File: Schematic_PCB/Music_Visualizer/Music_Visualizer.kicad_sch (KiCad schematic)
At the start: 145 parts, among them J1 AudioJack3, J3 Screw_Terminal_01x02, SW1 SW_SPDT, U1 LM324, U2 LM324, U3 LM324, U4 LM324, U5 LM324, U6 LM324, U7 LM324

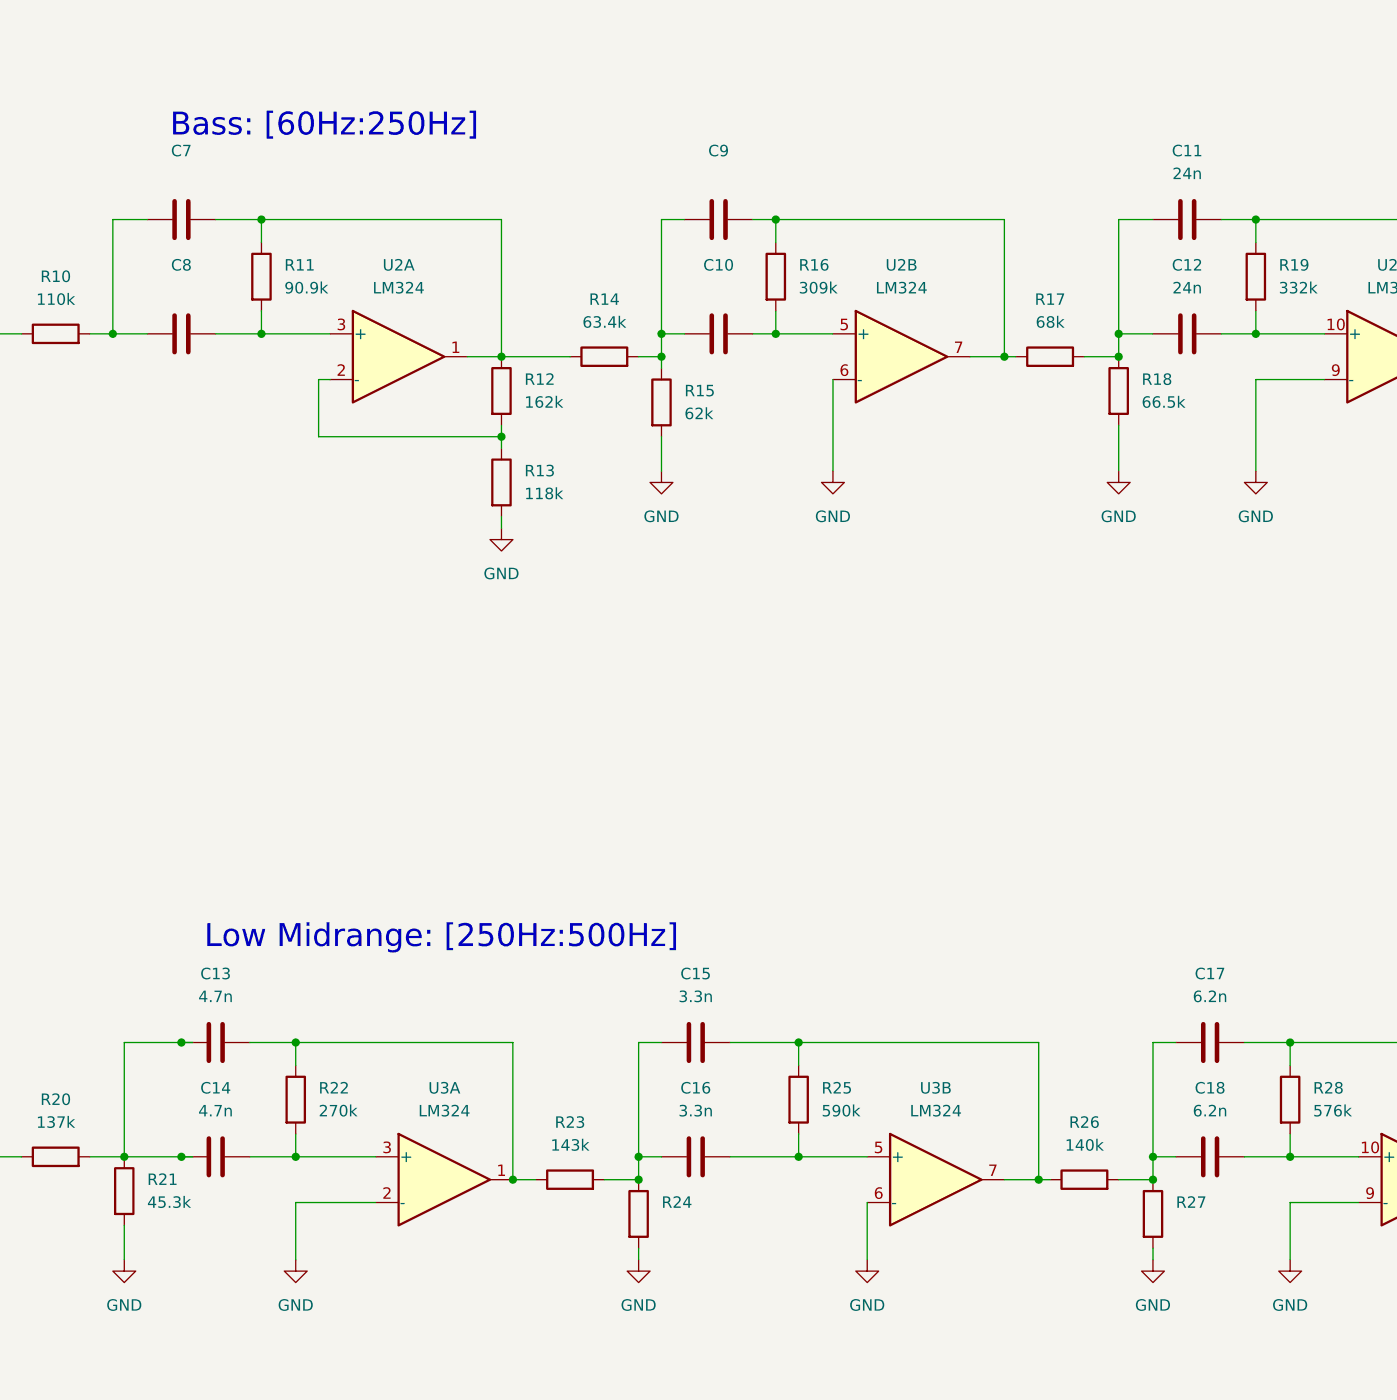
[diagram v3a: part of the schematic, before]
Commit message: Corrected LT1054 -5V power output label placement, identified which components are 0201 and corrected digi number and page of C-47,48,49,52,53,58 1u caps
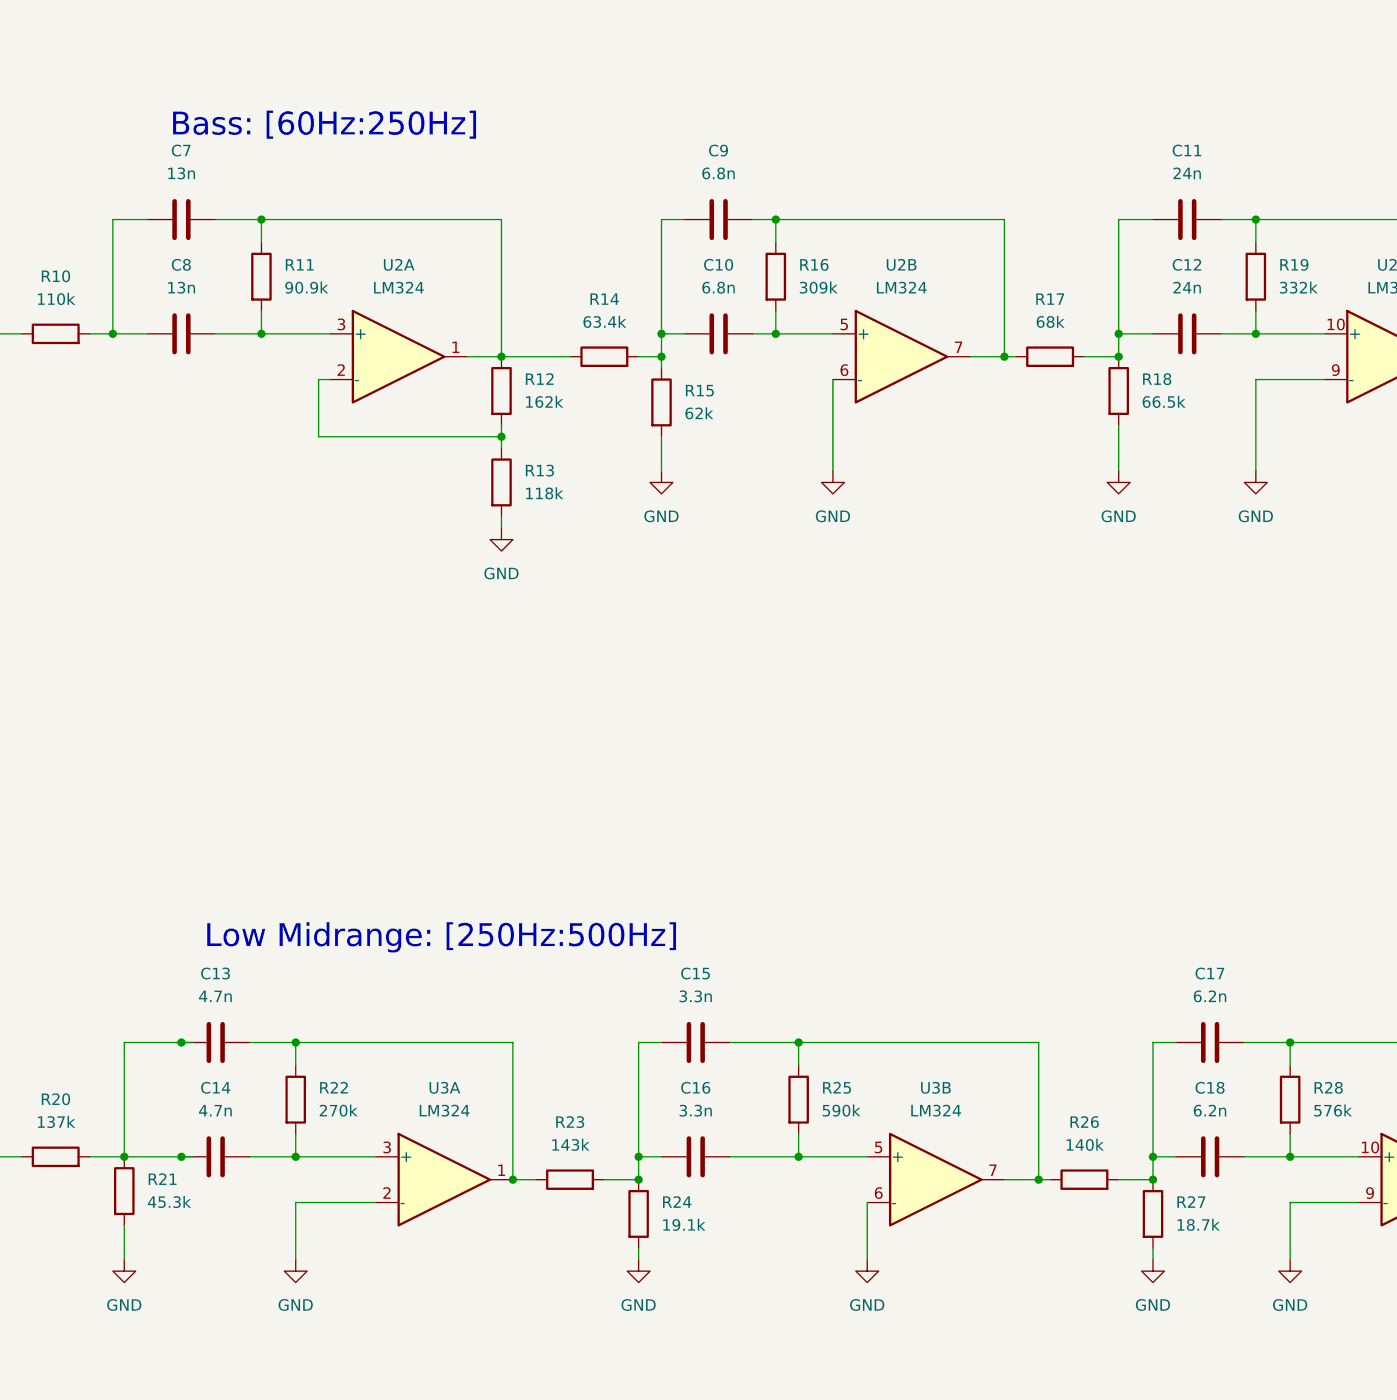
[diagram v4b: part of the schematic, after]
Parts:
- C10, C9: value (none) -> 6.8n; footprint (none) -> Capacitor_SMD:C_0805_2012Metric
- C7, C8: value (none) -> 13n; footprint (none) -> Capacitor_SMD:C_0805_2012Metric
- R24: value (none) -> 19.1k
- R27: value (none) -> 18.7k
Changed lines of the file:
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@@
     (in_bom yes) (on_board yes) (fields_autoplaced)
     (property "Reference" "C7" (id 0) (at 77.47 116.84 90))
-    (property "Value" "" (id 1) (at 77.47 119.38 90))
-    (property "Footprint" "" (id 2) (at 81.28 123.4948 0)
+    (property "Value" "13n" (id 1) (at 77.47 119.38 90))
+    (property "Footprint" "Capacitor_SMD:C_0805_2012Metric" (id 2) (at 81.28 123.4948 0)
       (effects (font (size 1.27 1.27)) hide)
     )
@@
       (effects (font (size 1.27 1.27)) (justify left))
     )
-    (property "Value" "" (id 1) (at 130.81 236.2199 0)
+    (property "Value" "19.1k" (id 1) (at 130.81 236.2199 0)
       (effects (font (size 1.27 1.27)) (justify left))
     )
@@
     (in_bom yes) (on_board yes) (fields_autoplaced)
     (property "Reference" "C10" (id 0) (at 137.16 129.54 90))
-    (property "Value" "" (id 1) (at 137.16 132.08 90))
-    (property "Footprint" "" (id 2) (at 140.97 136.1948 0)
+    (property "Value" "6.8n" (id 1) (at 137.16 132.08 90))
+    (property "Footprint" "Capacitor_SMD:C_0805_2012Metric" (id 2) (at 140.97 136.1948 0)
       (effects (font (size 1.27 1.27)) hide)
     )
@@
     (in_bom yes) (on_board yes) (fields_autoplaced)
     (property "Reference" "C9" (id 0) (at 137.16 116.84 90))
-    (property "Value" "" (id 1) (at 137.16 119.38 90))
-    (property "Footprint" "" (id 2) (at 140.97 123.4948 0)
+    (property "Value" "6.8n" (id 1) (at 137.16 119.38 90))
+    (property "Footprint" "Capacitor_SMD:C_0805_2012Metric" (id 2) (at 140.97 123.4948 0)
       (effects (font (size 1.27 1.27)) hide)
     )
@@
       (effects (font (size 1.27 1.27)) (justify left))
     )
-    (property "Value" "" (id 1) (at 187.96 236.2199 0)
+    (property "Value" "18.7k" (id 1) (at 187.96 236.2199 0)
       (effects (font (size 1.27 1.27)) (justify left))
     )
@@
     (in_bom yes) (on_board yes) (fields_autoplaced)
     (property "Reference" "C8" (id 0) (at 77.47 129.54 90))
-    (property "Value" "" (id 1) (at 77.47 132.08 90))
-    (property "Footprint" "" (id 2) (at 81.28 136.1948 0)
+    (property "Value" "13n" (id 1) (at 77.47 132.08 90))
+    (property "Footprint" "Capacitor_SMD:C_0805_2012Metric" (id 2) (at 81.28 136.1948 0)
       (effects (font (size 1.27 1.27)) hide)
     )
@@
       (reference "#FLG01") (unit 1) (value "PWR_FLAG") (footprint "")
     )
-    (path "/d77592bc-5812-4255-9ac4-28fcc93efec5/21a0d5b9-4532-462a-b222-783efa70e233"
-      (reference "#FLG02") (unit 1) (value "PWR_FLAG") (footprint "")
-    )
     (path "/d77592bc-5812-4255-9ac4-28fcc93efec5/fbbe1fa2-c5da-4d54-96b5-940791a713dd"
       (reference "#FLG03") (unit 1) (value "PWR_FLAG") (footprint "")
     )
+    (path "/d77592bc-5812-4255-9ac4-28fcc93efec5/edbb08b9-a6bc-45d0-889d-7924891dbc67"
+      (reference "#FLG?") (unit 1) (value "PWR_FLAG") (footprint "")
+    )
     (path "/5633cbad-15d0-469a-972b-d5c974b7291e"
       (reference "#PWR01") (unit 1) (value "GND") (footprint "")
@@
       (reference "#PWR056") (unit 1) (value "GND") (footprint "")
     )
-    (path "/d77592bc-5812-4255-9ac4-28fcc93efec5/e4fcda79-1137-4c2c-a9d6-4b6122edba87"
-      (reference "#PWR057") (unit 1) (value "-5V") (footprint "")
-    )
     (path "/d77592bc-5812-4255-9ac4-28fcc93efec5/ac53abec-9b90-408c-8fa1-04c26bd4ed05"
       (reference "#PWR058") (unit 1) (value "+9V") (footprint "")
@@
       (reference "#PWR0112") (unit 1) (value "-5V") (footprint "")
     )
+    (path "/d77592bc-5812-4255-9ac4-28fcc93efec5/efa0b5dd-fae2-4f37-86f2-2228dd6f0e00"
+      (reference "#PWR?") (unit 1) (value "-5V") (footprint "")
+    )
     (path "/d3791e18-fb94-4a94-9f9d-30d4fd98db8e"

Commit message: Re-organized Sub-bass and Bass part of the PCB
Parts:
- C1, C2: value 47n -> (none); footprint Capacitor_SMD:C_0201_0603Metric -> (none)
- C13, C14: value 4.7n -> (none); footprint Capacitor_SMD:C_0201_0603Metric -> (none)
- C15, C16: value 3.3n -> (none); footprint Capacitor_SMD:C_0201_0603Metric -> (none)
- C21, C22, C25, C26, C27, C28, C29, C30, C31, C32, C33, C34, C35, C36, C37, C38, C39, C40, C41, C42: value 1n -> (none); footprint Capacitor_SMD:C_0201_0603Metric -> (none)
- C3, C4: value 27n -> (none); footprint Capacitor_SMD:C_0603_1608Metric -> (none)
- R1: value 84.5k -> (none); footprint Resistor_SMD:R_0201_0603Metric -> (none)
- R10: value 110k -> (none); footprint Resistor_SMD:R_0201_0603Metric -> (none)
- R11, R4, R65: value 90.9k -> (none); footprint Resistor_SMD:R_0201_0603Metric -> (none)
- R12: value 162k -> (none); footprint Resistor_SMD:R_0201_0603Metric -> (none)
- R13: value 118k -> (none); footprint Resistor_SMD:R_0201_0603Metric -> (none)
- R14: value 63.4k -> (none); footprint Resistor_SMD:R_0201_0603Metric -> (none)
- R15: value 62k -> (none); footprint Resistor_SMD:R_0201_0603Metric -> (none)
- R16: value 309k -> (none); footprint Resistor_SMD:R_0201_0603Metric -> (none)
- R17: value 68k -> (none); footprint Resistor_SMD:R_0201_0603Metric -> (none)
- R18, R31, R36, R51: value 66.5k -> (none); footprint Resistor_SMD:R_0201_0603Metric -> (none)
- R19: value 332k -> (none); footprint Resistor_SMD:R_0201_0603Metric -> (none)
- R2, R41, R50: value 160k -> (none); footprint Resistor_SMD:R_0201_0603Metric -> (none)
- R20: value 137k -> (none); footprint Resistor_SMD:R_0201_0603Metric -> (none)
- R21: value 45.3k -> (none); footprint Resistor_SMD:R_0201_0603Metric -> (none)
- R22, R35, R53: value 270k -> (none); footprint Resistor_SMD:R_0201_0603Metric -> (none)
- R23: value 143k -> (none); footprint Resistor_SMD:R_0201_0603Metric -> (none)
- R24: value 19.1k -> (none); footprint Resistor_SMD:R_0201_0603Metric -> (none)
- R25: value 590k -> (none); footprint Resistor_SMD:R_0201_0603Metric -> (none)
- R26: value 140k -> (none); footprint Resistor_SMD:R_0201_0603Metric -> (none)
- R27: value 18.7k -> (none); footprint Resistor_SMD:R_0201_0603Metric -> (none)
- R28: value 576k -> (none); footprint Resistor_SMD:R_0201_0603Metric -> (none)
- R29, R30: value 100k -> (none); footprint Resistor_SMD:R_0201_0603Metric -> (none)
- R3: value 169k -> (none); footprint Resistor_SMD:R_0201_0603Metric -> (none)
- R32: value 33.2k -> (none); footprint Resistor_SMD:R_0201_0603Metric -> (none)
- R33: value 56k -> (none); footprint Resistor_SMD:R_0201_0603Metric -> (none)
- R34, R58: value 48.7k -> (none); footprint Resistor_SMD:R_0201_0603Metric -> (none)
- R37: value 57.6k -> (none); footprint Resistor_SMD:R_0201_0603Metric -> (none)
- R38: value 324k -> (none); footprint Resistor_SMD:R_0201_0603Metric -> (none)
- R39, R48: value 78.7k -> (none); footprint Resistor_SMD:R_0201_0603Metric -> (none)
- R40: value 26.7k -> (none); footprint Resistor_SMD:R_0201_0603Metric -> (none)
- R42: value 59k -> (none); footprint Resistor_SMD:R_0201_0603Metric -> (none)
- R43: value 7.87k -> (none); footprint Resistor_SMD:R_0201_0603Metric -> (none)
- R44: value 243k -> (none); footprint Resistor_SMD:R_0201_0603Metric -> (none)
- R45: value 107k -> (none); footprint Resistor_SMD:R_0201_0603Metric -> (none)
- R46: value 14.7k -> (none); footprint Resistor_SMD:R_0201_0603Metric -> (none)
- R47: value 453k -> (none); footprint Resistor_SMD:R_0201_0603Metric -> (none)
- R49: value 7.32k -> (none); footprint Resistor_SMD:R_0201_0603Metric -> (none)
- R5, R62: value 37.4k -> (none); footprint Resistor_SMD:R_0201_0603Metric -> (none)
- R52: value 2.87k -> (none); footprint Resistor_SMD:R_0201_0603Metric -> (none)
- R54: value 95.3k -> (none); footprint Resistor_SMD:R_0201_0603Metric -> (none)
- R55: value 4.02k -> (none); footprint Resistor_SMD:R_0201_0603Metric -> (none)
- R56: value 383k -> (none); footprint Resistor_SMD:R_0201_0603Metric -> (none)
- R59: value 22.6k -> (none); footprint Resistor_SMD:R_0201_0603Metric -> (none)
- R6: value 402k -> (none); footprint Resistor_SMD:R_0201_0603Metric -> (none)
- R60: value 8.06k -> (none); footprint Resistor_SMD:R_0201_0603Metric -> (none)
- R61: value 4.32k -> (none); footprint Resistor_SMD:R_0201_0603Metric -> (none)
- R63: value 19.6k -> (none); footprint Resistor_SMD:R_0201_0603Metric -> (none)
- R64: value 10.7k -> (none); footprint Resistor_SMD:R_0201_0603Metric -> (none)
- R66, R67, R68, R69, R70, R71, R72: value 1k -> (none); footprint Resistor_SMD:R_0201_0603Metric -> (none)
- R7: value 86.6k -> (none); footprint Resistor_SMD:R_0201_0603Metric -> (none)
- R8: value 35.7k -> (none); footprint Resistor_SMD:R_0201_0603Metric -> (none)
- R9: value 390k -> (none); footprint Resistor_SMD:R_0201_0603Metric -> (none)

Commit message: Changed 0603 footprint to hand solder version, and changed 0402 footprints to 0603 hand solder version
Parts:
- C1, C2: value (none) -> 47n; footprint (none) -> Capacitor_SMD:C_0603_1608Metric_Pad1.08x0.95mm_HandSolder
- C13, C14: value (none) -> 4.7n; footprint (none) -> Capacitor_SMD:C_0603_1608Metric_Pad1.08x0.95mm_HandSolder
- C15, C16: value (none) -> 3.3n; footprint (none) -> Capacitor_SMD:C_0603_1608Metric_Pad1.08x0.95mm_HandSolder
- C19, C20: value 1.6n -> (none); footprint Capacitor_SMD:C_0603_1608Metric -> (none)
- C21, C22, C25, C26, C27, C28, C29, C30, C31, C32, C33, C34, C35, C36, C37, C38, C39, C40, C41, C42: value (none) -> 1n; footprint (none) -> Capacitor_SMD:C_0603_1608Metric_Pad1.08x0.95mm_HandSolder
- C23, C24: value 3n -> (none); footprint Capacitor_SMD:C_0402_1005Metric -> (none)
- C3: value (none) -> 27n; footprint (none) -> Capacitor_SMD:C_0603_1608Metric_Pad1.08x0.95mm_HandSolder
- C47, C48, C49: value 1u -> (none); footprint Capacitor_SMD:C_0402_1005Metric -> (none)
- R1: value (none) -> 84.5k; footprint (none) -> Capacitor_SMD:C_0603_1608Metric_Pad1.08x0.95mm_HandSolder
- R10: value (none) -> 110k; footprint (none) -> Capacitor_SMD:C_0603_1608Metric_Pad1.08x0.95mm_HandSolder
- R11, R4, R65: value (none) -> 90.9k; footprint (none) -> Capacitor_SMD:C_0603_1608Metric_Pad1.08x0.95mm_HandSolder
- R12: value (none) -> 162k; footprint (none) -> Capacitor_SMD:C_0603_1608Metric_Pad1.08x0.95mm_HandSolder
- R13: value (none) -> 118k; footprint (none) -> Capacitor_SMD:C_0603_1608Metric_Pad1.08x0.95mm_HandSolder
- R14: value (none) -> 63.4k; footprint (none) -> Capacitor_SMD:C_0603_1608Metric_Pad1.08x0.95mm_HandSolder
- R15: value (none) -> 62k; footprint (none) -> Capacitor_SMD:C_0603_1608Metric_Pad1.08x0.95mm_HandSolder
- R16: value (none) -> 309k; footprint (none) -> Capacitor_SMD:C_0603_1608Metric_Pad1.08x0.95mm_HandSolder
- R17: value (none) -> 68k; footprint (none) -> Capacitor_SMD:C_0603_1608Metric_Pad1.08x0.95mm_HandSolder
- R18, R31, R36, R51: value (none) -> 66.5k; footprint (none) -> Capacitor_SMD:C_0603_1608Metric_Pad1.08x0.95mm_HandSolder
- R19: value (none) -> 332k; footprint (none) -> Capacitor_SMD:C_0603_1608Metric_Pad1.08x0.95mm_HandSolder
- R2, R41, R50: value (none) -> 160k; footprint (none) -> Capacitor_SMD:C_0603_1608Metric_Pad1.08x0.95mm_HandSolder
- R20: value (none) -> 137k; footprint (none) -> Capacitor_SMD:C_0603_1608Metric_Pad1.08x0.95mm_HandSolder
- R21: value (none) -> 45.3k; footprint (none) -> Capacitor_SMD:C_0603_1608Metric_Pad1.08x0.95mm_HandSolder
- R22, R35, R53: value (none) -> 270k; footprint (none) -> Capacitor_SMD:C_0603_1608Metric_Pad1.08x0.95mm_HandSolder
- R23: value (none) -> 143k; footprint (none) -> Capacitor_SMD:C_0603_1608Metric_Pad1.08x0.95mm_HandSolder
- R24: value (none) -> 19.1k; footprint (none) -> Capacitor_SMD:C_0603_1608Metric_Pad1.08x0.95mm_HandSolder
- R25: value (none) -> 590k; footprint (none) -> Capacitor_SMD:C_0603_1608Metric_Pad1.08x0.95mm_HandSolder
- R26: value (none) -> 140k; footprint (none) -> Capacitor_SMD:C_0603_1608Metric_Pad1.08x0.95mm_HandSolder
- R27: value (none) -> 18.7k; footprint (none) -> Capacitor_SMD:C_0603_1608Metric_Pad1.08x0.95mm_HandSolder
- R28: value (none) -> 576k; footprint (none) -> Capacitor_SMD:C_0603_1608Metric_Pad1.08x0.95mm_HandSolder
- R29, R30: value (none) -> 100k; footprint (none) -> Capacitor_SMD:C_0603_1608Metric_Pad1.08x0.95mm_HandSolder
- R3: value (none) -> 169k; footprint (none) -> Capacitor_SMD:C_0603_1608Metric_Pad1.08x0.95mm_HandSolder
- R32: value (none) -> 33.2k; footprint (none) -> Capacitor_SMD:C_0603_1608Metric_Pad1.08x0.95mm_HandSolder
- R33: value (none) -> 56k; footprint (none) -> Capacitor_SMD:C_0603_1608Metric_Pad1.08x0.95mm_HandSolder
- R34, R58: value (none) -> 48.7k; footprint (none) -> Capacitor_SMD:C_0603_1608Metric_Pad1.08x0.95mm_HandSolder
- R37: value (none) -> 57.6k; footprint (none) -> Capacitor_SMD:C_0603_1608Metric_Pad1.08x0.95mm_HandSolder
- R38: value (none) -> 324k; footprint (none) -> Capacitor_SMD:C_0603_1608Metric_Pad1.08x0.95mm_HandSolder
- R39, R48: value (none) -> 78.7k; footprint (none) -> Capacitor_SMD:C_0603_1608Metric_Pad1.08x0.95mm_HandSolder
- R40: value (none) -> 26.7k; footprint (none) -> Capacitor_SMD:C_0603_1608Metric_Pad1.08x0.95mm_HandSolder
- R42: value (none) -> 59k; footprint (none) -> Capacitor_SMD:C_0603_1608Metric_Pad1.08x0.95mm_HandSolder
- R43: value (none) -> 7.87k; footprint (none) -> Capacitor_SMD:C_0603_1608Metric_Pad1.08x0.95mm_HandSolder
- R44: value (none) -> 243k; footprint (none) -> Capacitor_SMD:C_0603_1608Metric_Pad1.08x0.95mm_HandSolder
- R45: value (none) -> 107k; footprint (none) -> Capacitor_SMD:C_0603_1608Metric_Pad1.08x0.95mm_HandSolder
- R46: value (none) -> 14.7k; footprint (none) -> Capacitor_SMD:C_0603_1608Metric_Pad1.08x0.95mm_HandSolder
- R47: value (none) -> 453k; footprint (none) -> Capacitor_SMD:C_0603_1608Metric_Pad1.08x0.95mm_HandSolder
- R49: value (none) -> 7.32k; footprint (none) -> Capacitor_SMD:C_0603_1608Metric_Pad1.08x0.95mm_HandSolder
- R5, R62: value (none) -> 37.4k; footprint (none) -> Capacitor_SMD:C_0603_1608Metric_Pad1.08x0.95mm_HandSolder
- R52: value (none) -> 2.87k; footprint (none) -> Capacitor_SMD:C_0603_1608Metric_Pad1.08x0.95mm_HandSolder
- R54: value (none) -> 95.3k; footprint (none) -> Capacitor_SMD:C_0603_1608Metric_Pad1.08x0.95mm_HandSolder
- R55: value (none) -> 4.02k; footprint (none) -> Capacitor_SMD:C_0603_1608Metric_Pad1.08x0.95mm_HandSolder
- R56: value (none) -> 383k; footprint (none) -> Capacitor_SMD:C_0603_1608Metric_Pad1.08x0.95mm_HandSolder
- R59: value (none) -> 22.6k; footprint (none) -> Capacitor_SMD:C_0603_1608Metric_Pad1.08x0.95mm_HandSolder
- R6: value (none) -> 402k; footprint (none) -> Capacitor_SMD:C_0603_1608Metric_Pad1.08x0.95mm_HandSolder
- R60: value (none) -> 8.06k; footprint (none) -> Capacitor_SMD:C_0603_1608Metric_Pad1.08x0.95mm_HandSolder
- R61: value (none) -> 4.32k; footprint (none) -> Capacitor_SMD:C_0603_1608Metric_Pad1.08x0.95mm_HandSolder
- R63: value (none) -> 19.6k; footprint (none) -> Capacitor_SMD:C_0603_1608Metric_Pad1.08x0.95mm_HandSolder
- R64: value (none) -> 10.7k; footprint (none) -> Capacitor_SMD:C_0603_1608Metric_Pad1.08x0.95mm_HandSolder
- R66, R67, R68, R69, R70, R71, R72: value (none) -> 1k; footprint (none) -> Capacitor_SMD:C_0603_1608Metric_Pad1.08x0.95mm_HandSolder
- R7: value (none) -> 86.6k; footprint (none) -> Capacitor_SMD:C_0603_1608Metric_Pad1.08x0.95mm_HandSolder
- R8: value (none) -> 35.7k; footprint (none) -> Capacitor_SMD:C_0603_1608Metric_Pad1.08x0.95mm_HandSolder
- R9: value (none) -> 390k; footprint (none) -> Capacitor_SMD:C_0603_1608Metric_Pad1.08x0.95mm_HandSolder
